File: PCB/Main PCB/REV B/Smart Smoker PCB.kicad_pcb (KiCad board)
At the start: 4 copper layers, 102 parts, among them J1 105017-0001, J10 MEM2051-00-195-00-A, J11 Hopper, J12 Lid, J2 HEATER, J3 393570002, J4 AUGER, J5 393570002, J6 393570002, J7 393570002, J8 393570002, J9 FAN, Q1 25V 1.5A Trans, Q2 25V 1.5A Trans, Q3 Q_PMOS_GSD, Q4 Q_PMOS_GSD, SW1 SW_Coded_SH-7050, U1 AMS1117-3.3, U2 CP2102N-Axx-xQFN20, U3 DG409LEDY-T1-GE3, U4 MAX31855KASA, U5 ESP32-WROOM-32UE_16MB, U6 CPC1966B, U7 AQH2223A, U8 LTC4412xS6, U9 AQH2223A

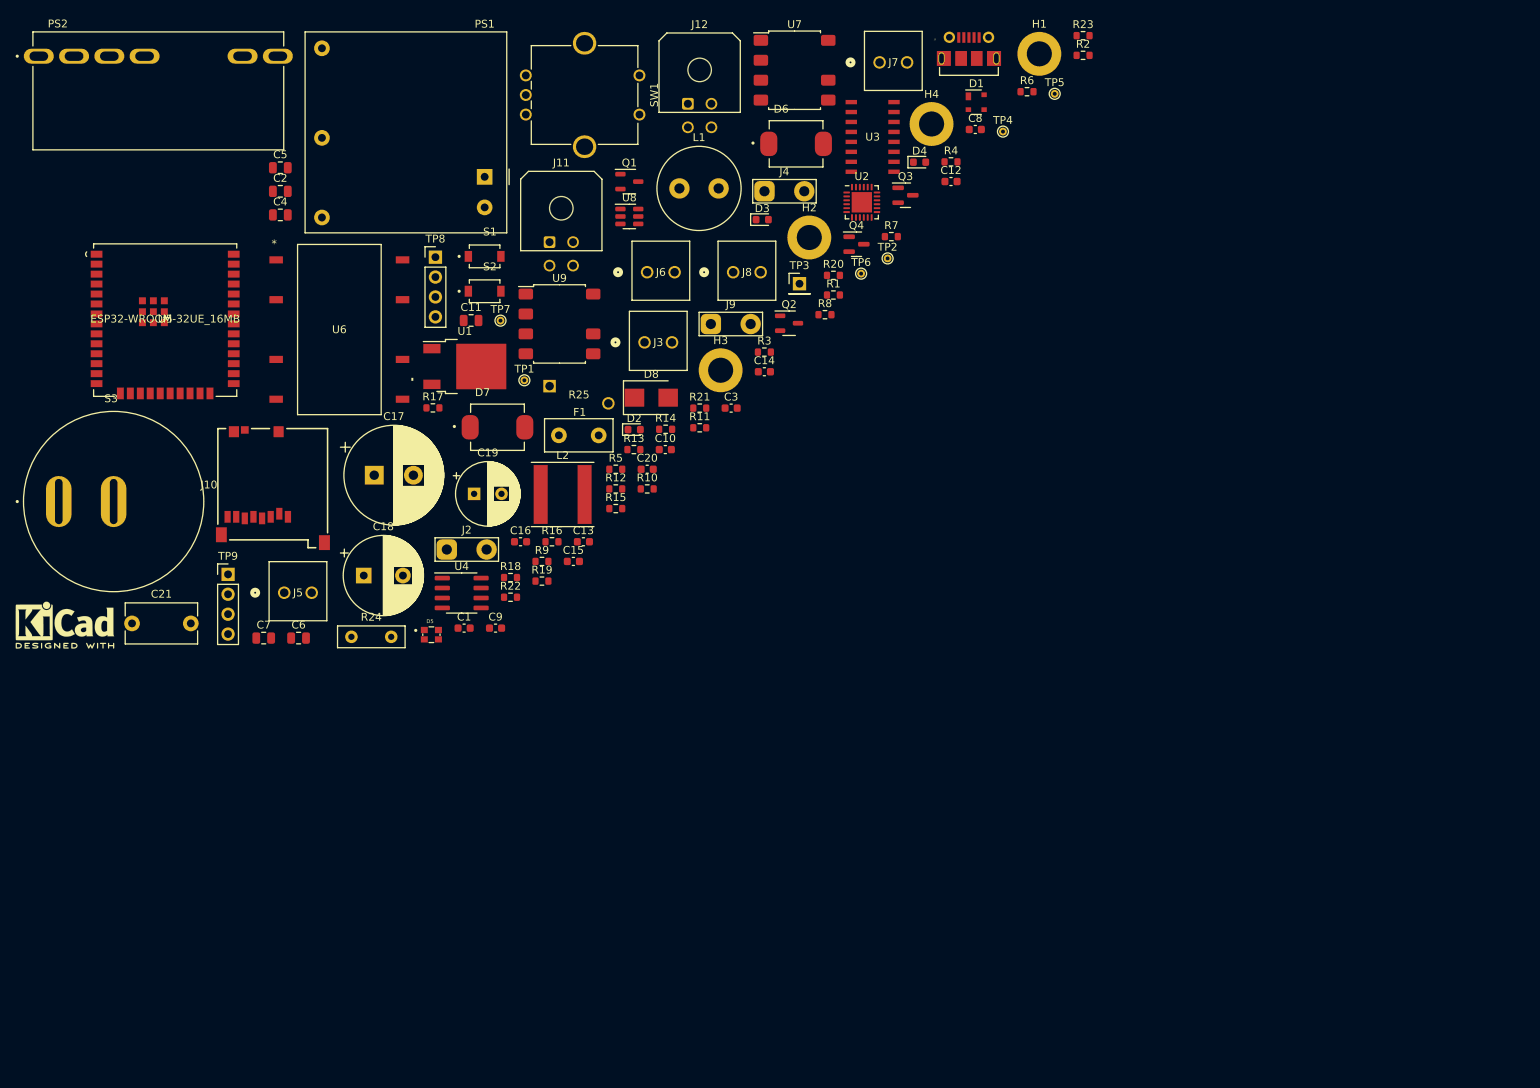
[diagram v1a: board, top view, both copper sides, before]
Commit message: Rev B Hardware - organization of schematic and initial layout for board sizing
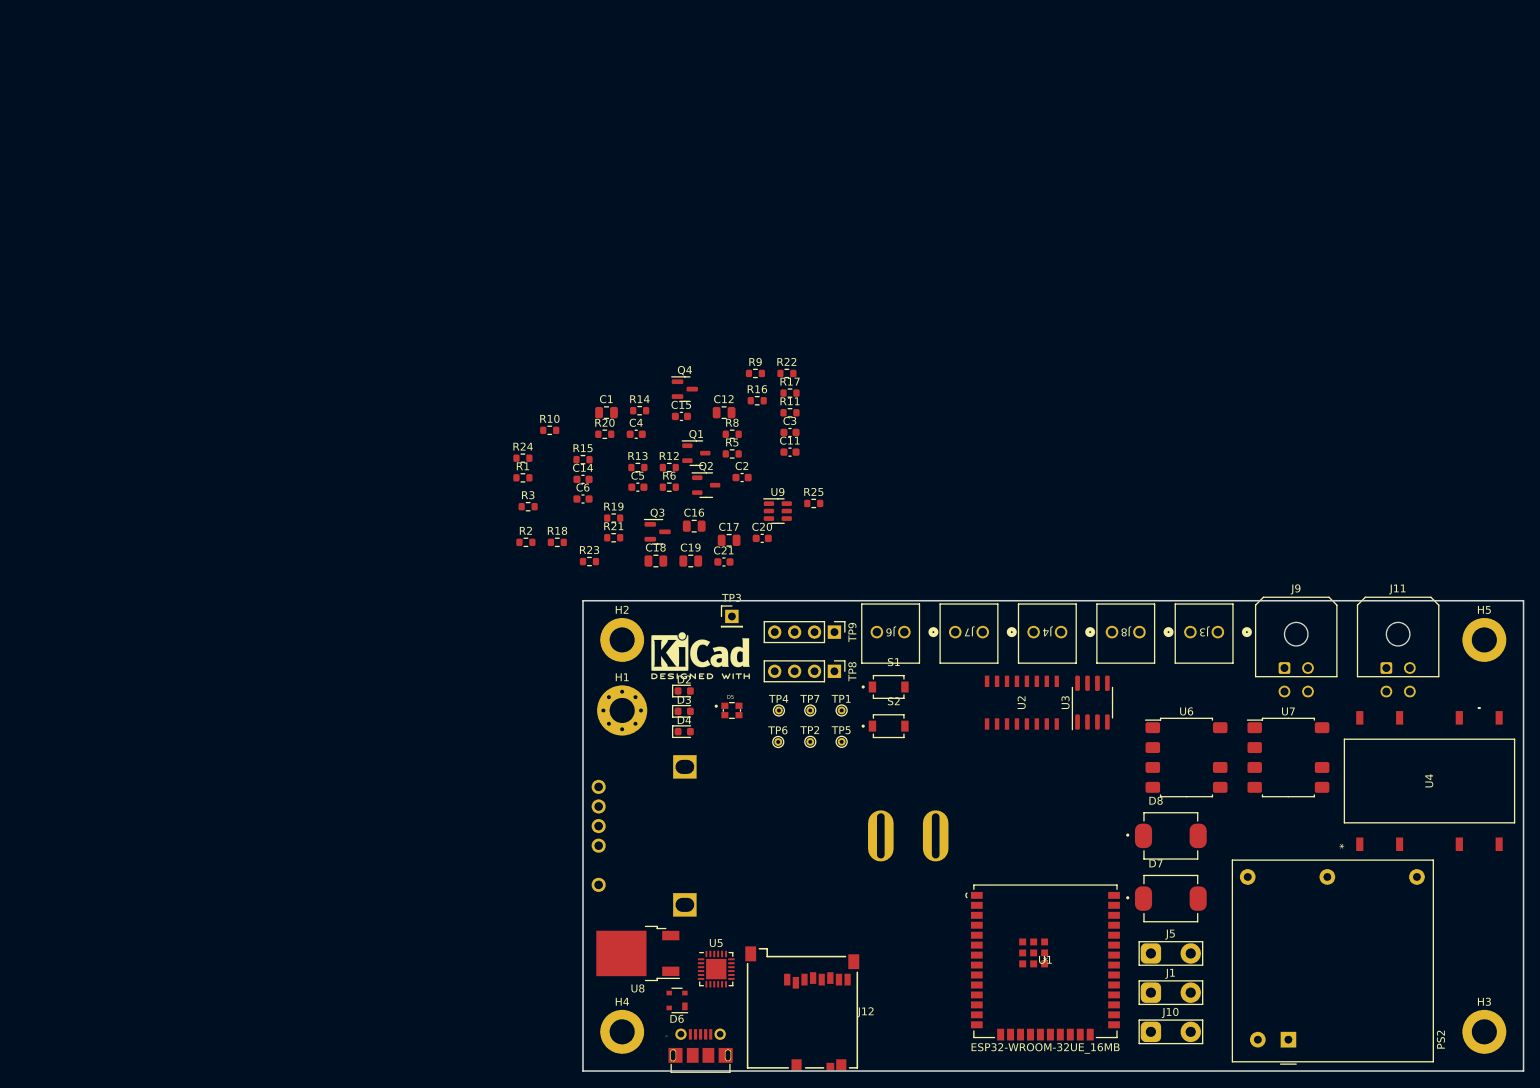
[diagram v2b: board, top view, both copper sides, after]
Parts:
- removed C10: 0.01uF 50V X7R 0603, Capacitor_SMD:C_0603_1608Metric
- removed C13, C8, C9: 0.1uF 50V X7R 0603, Capacitor_SMD:C_0603_1608Metric
- removed C7: 10uF 16V X5R 0805, Capacitor_SMD:C_0805_2012Metric
- removed D1: SP0503BAHT, Package_TO_SOT_SMD:SOT-143
- removed F1: 300V 2A SlowBlow, Fuse:Fuse_Littelfuse_395Series
- removed L1: 2.2mH 500mA 2.5Ohm TH, Inductor_THT:L_Radial_D10.5mm_P5.00mm_Abacron_AISR-01
- removed L2: 2.2uH 7.2A 11.5mOhm, Inductor_SMD:L_Taiyo-Yuden_NR-80xx
- removed PS1: RAC05-3.3SK, Converter_ACDC:Converter_ACDC_RECOM_RAC05-xxSK_THT
- removed R4: 10K 1% 0603, Resistor_SMD:R_0603_1608Metric
- removed R7: 0Ohm 0603, Resistor_SMD:R_0603_1608Metric
- added H5: MountingHole, MountingHole:MountingHole_3.2mm_M3_DIN965_Pad, F.Cu at (215.0, 105.0)
- C1: value 0.1uF 50V X7R 0603 -> 22uF 10V X5R 0805; footprint Capacitor_SMD:C_0603_1608Metric -> Capacitor_SMD:C_0805_2012Metric
- C11: value 22uF 10V X5R 0805 -> 0.1uF 50V X7R 0603; footprint Capacitor_SMD:C_0805_2012Metric -> Capacitor_SMD:C_0603_1608Metric
- C12: value 0.1uF 50V X7R 0603 -> 4.7uF 25V X5R 0805; footprint Capacitor_SMD:C_0603_1608Metric -> Capacitor_SMD:C_0805_2012Metric
- C15: value 1uF 25V X5R 0603 -> 0.1uF 50V X7R 0603
- C16: value 0.1uF 50V X7R 0603 -> 10uF 16V X5R 0805; footprint Capacitor_SMD:C_0603_1608Metric -> Capacitor_SMD:C_0805_2012Metric
- C17: value 22uF 450V 20% -> 10uF 16V X5R 0805; footprint Capacitor_THT:CP_Radial_D12.5mm_P5.00mm -> Capacitor_SMD:C_0805_2012Metric
- C18: value 820uF 20% 16V -> 10uF 16V X5R 0805; footprint Capacitor_THT:CP_Radial_D10.0mm_P5.00mm -> Capacitor_SMD:C_0805_2012Metric
- C19: value 150uF 20% 35V -> 10uF 16V X5R 0805; footprint Capacitor_THT:CP_Radial_D8.0mm_P3.50mm -> Capacitor_SMD:C_0805_2012Metric
- C2: value 4.7uF 25V X5R 0805 -> 0.1uF 50V X7R 0603; footprint Capacitor_SMD:C_0805_2012Metric -> Capacitor_SMD:C_0603_1608Metric
- C20: value 0.1uF 50V X7R 0603 -> 1uF 25V X5R 0603
- C21: value 1000pF 440VAC Y5P -> 0.1uF 50V X7R 0603; footprint Capacitor_THT:C_Disc_D9.0mm_W5.0mm_P7.50mm -> Capacitor_SMD:C_0603_1608Metric
- C4: value 10uF 16V X5R 0805 -> 0.01uF 50V X7R 0603; footprint Capacitor_SMD:C_0805_2012Metric -> Capacitor_SMD:C_0603_1608Metric
- C5, C6: value 10uF 16V X5R 0805 -> 0.1uF 50V X7R 0603; footprint Capacitor_SMD:C_0805_2012Metric -> Capacitor_SMD:C_0603_1608Metric
- D6: value D_TVS -> SP0503BAHT; footprint Customs Smoker:DIOM7959X262N -> Package_TO_SOT_SMD:SOT-143
- D8: value TVS DIODE 7VWM 12VC SMB -> D_TVS; footprint Diode_SMD:D_SMB -> Customs Smoker:DIOM7959X262N
- H1: value MountingHole -> AC_GND; footprint MountingHole:MountingHole_3.2mm_M3_DIN965_Pad -> MountingHole:MountingHole_3.2mm_M3_Pad_Via
- J1: value 105017-0001 -> HEATER; footprint Customs Smoker:MOLEX_105017-0001 -> TestPoint:TestPoint_2Pads_Pitch5.08mm_Drill1.3mm
- J10: value MEM2051-00-195-00-A -> FAN; footprint Customs Smoker:GCT_MEM2051-00-195-00-A -> TestPoint:TestPoint_2Pads_Pitch5.08mm_Drill1.3mm
- J11: value Hopper -> Lid
- J12: value Lid -> MEM2051-00-195-00-A; footprint Connector_Molex:Molex_Micro-Fit_3.0_43045-0400_2x02_P3.00mm_Horizontal -> Customs Smoker:GCT_MEM2051-00-195-00-A
- J2: value HEATER -> 105017-0001; footprint TestPoint:TestPoint_2Pads_Pitch5.08mm_Drill1.3mm -> Customs Smoker:MOLEX_105017-0001
- J4: value AUGER -> 393570002; footprint TestPoint:TestPoint_2Pads_Pitch5.08mm_Drill1.3mm -> Customs Smoker:CONN_393570002_MOL
- J5: value 393570002 -> AUGER; footprint Customs Smoker:CONN_393570002_MOL -> TestPoint:TestPoint_2Pads_Pitch5.08mm_Drill1.3mm
- J9: value FAN -> Hopper; footprint TestPoint:TestPoint_2Pads_Pitch5.08mm_Drill1.3mm -> Connector_Molex:Molex_Micro-Fit_3.0_43045-0400_2x02_P3.00mm_Horizontal
- PS2: value LS10-13B03R3 -> RAC05-3.3SK; footprint Customs Smoker:CONV_LS10-13B03R3 -> Converter_ACDC:Converter_ACDC_RECOM_RAC05-xxSK_THT
- R1: value 1kOhm 1% 0603 -> 1.8kOhm 1% 0603
- R11: value 470Ohm 1% 0603 -> 750Ohm 1% 0603
- R13: value 140Ohm 1% 0603 -> 22.1kOhm 1% 0603
- R14: value 750Ohm 1% 0603 -> 20Ohm 1% 0603
- R15: value 80.6Ohm 1% 0603 -> 20Ohm 1% 0603
- R16: value 20Ohm 1% 0603 -> 80.6Ohm 1% 0603
- R17: value 20Ohm 1% 0603 -> 64.9Ohm 1% 0603
- R18: value 64.9Ohm 1% 0603 -> 0Ohm 0603
- R19: value 140Ohm 1% 0603 -> 47.5kOhm 1% 0603
- R2: value 10K 1% 0603 -> 1.8kOhm 1% 0603
- R20: value 80.6Ohm 1% 0603 -> 0Ohm 0603
- R21: value 470Ohm 5% 0603 -> 140Ohm 1% 0603
- R22: value 140Ohm 1% 0603 -> 80.6Ohm 1% 0603
- R23: value 80.6Ohm 1% 0603 -> 140Ohm 1% 0603
- R24: value 6.8Ohm 3W 5% 2512 -> 80.6Ohm 1% 0603; footprint Resistor_THT:R_Box_L8.4mm_W2.5mm_P5.08mm -> Resistor_SMD:R_0603_1608Metric
- R25: value B72214S0351K101 -> 470Ohm 5% 0603; footprint Customs Smoker:VARS_B72214S_15P5X5P6-7P5-2P2_TDK -> Resistor_SMD:R_0603_1608Metric
- R3: value 22.1kOhm 1% 0603 -> 10K 1% 0603
- R5: value 47.5kOhm 1% 0603 -> 470Ohm 1% 0603
- R6: value 0Ohm 0603 -> 10K 1% 0603
- R8: value 1.8kOhm 1% 0603 -> 1kOhm 1% 0603
- R9: value 1.8kOhm 1% 0603 -> 140Ohm 1% 0603
- S3: moved to B.Cu
- SW1: footprint Rotary_Encoder:RotaryEncoder_Bourns_Vertical_PEC12R-3xxxF-Sxxxx -> Rotary_Encoder:PAC18R1-43D19F; moved to B.Cu
- U1: value AMS1117-3.3 -> ESP32-WROOM-32UE_16MB; footprint Package_TO_SOT_SMD:TO-252-2 -> Customs Smoker:ESP32-WROOM-32UE 16MB
- U2: value CP2102N-Axx-xQFN20 -> DG409LEDY-T1-GE3; footprint Package_DFN_QFN:QFN-24-1EP_4x4mm_P0.5mm_EP2.6x2.6mm -> Customs Smoker:SOIC16_NARROW_VIS
- U3: value DG409LEDY-T1-GE3 -> MAX31855KASA; footprint Customs Smoker:SOIC16_NARROW_VIS -> Package_SO:SOIC-8_3.9x4.9mm_P1.27mm
- U4: value MAX31855KASA -> CPC1966B; footprint Package_SO:SOIC-8_3.9x4.9mm_P1.27mm -> Customs Smoker:CPC1966B_IXY
- U5: value ESP32-WROOM-32UE_16MB -> CP2102N-Axx-xQFN20; footprint Customs Smoker:ESP32-WROOM-32UE 16MB -> Package_DFN_QFN:QFN-24-1EP_4x4mm_P0.5mm_EP2.6x2.6mm
- U6: value CPC1966B -> AQH2223A; footprint Customs Smoker:CPC1966B_IXY -> Package_SO:SSO-7-8_6.4x9.78mm_P2.54mm
- U8: value LTC4412xS6 -> AMS1117-3.3; footprint Package_TO_SOT_SMD:TSOT-23-6 -> Package_TO_SOT_SMD:TO-252-2
- U9: value AQH2223A -> LTC4412xS6; footprint Package_SO:SSO-7-8_6.4x9.78mm_P2.54mm -> Package_TO_SOT_SMD:TSOT-23-6
- moved PS2 191.1 mm to (190.0, 156.0), turned to -90 degrees
- moved J10 131.8 mm to (172.5, 155.0)
- moved H3 128.9 mm to (215.0, 155.0)
- moved U4 125.8 mm to (208.0, 123.0), turned to 90 degrees
- moved H4 122.4 mm to (105.0, 155.0)
- moved J1 121.4 mm to (172.5, 150.0)
- moved U6 121.1 mm to (177.0, 120.0)
- moved J11 119.8 mm to (202.5, 108.6)
- moved J5 119.8 mm to (172.5, 145.0)
- moved J12 116.3 mm to (128.0, 152.0), turned to 180 degrees
- moved D6 110.3 mm to (112.0, 151.0), turned to 180 degrees
- moved U5 108.6 mm to (117.0, 147.0)
- moved U7 108.0 mm to (190.0, 120.0)
- moved S3 106.8 mm to (138.0, 130.0), turned to 180 degrees
- moved U1 106.0 mm to (159.0, 146.0)
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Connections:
- C14 pad 1: /IO0 -> +5V
- C15 pad 2: +3.3V -> +3.3VA
- C17 pad 1: Net-(C17-Pad1) -> +5V
- C17 pad 2: Net-(C17-Pad2) -> GND
- C18 pad 1: Net-(C18-Pad1) -> +3.3VP
- C19 pad 1: +3.3VA -> +3.3VP
- C20 pad 1: +3.3VA -> GND
- C20 pad 2: GND -> +3.3V
- C21 pad 1: Net-(C17-Pad2) -> +3.3VA
- C3 pad 1: Net-(C3-Pad1) -> +3.3V
- C3 pad 2: Net-(C3-Pad2) -> GND
- C4 pad 1: Net-(C3-Pad2) -> /MUX_OUT_+
- C4 pad 2: Net-(C3-Pad1) -> /MUX_OUT_-
- C5 pad 1: +5V -> /EN
- C6 pad 1: +3.3VP -> /IO0
- D6 pad 1: /Auger_+ -> GND
- D6 pad 2: /AC_L -> /USB_DP
- D7 pad 1: /Fan_+ -> /Auger_+
- D8 pad 1: GND -> /Fan_+
- D8 pad 2: +3.3VA -> /AC_L
- H1 pad 1: (no net) -> GND
- J1 pad 1: +5V -> /Heater_+
- J1 pad 2: /USB_DN -> /AC_N
- J10 pad 1: unconnected-(J10-Pad1) -> /Fan_+
- J10 pad 2: unconnected-(J10-Pad2) -> /AC_N
- J12 pad 1: /I2C_SDA -> unconnected-(J12-Pad1)
- J12 pad 2: GND -> unconnected-(J12-Pad2)
- J12 pad 3: /I2C_SCL -> unconnected-(J12-Pad3)
- J12 pad 4: +3.3V -> unconnected-(J12-Pad4)
- J2 pad 1: /Heater_+ -> +5V
- J2 pad 2: /AC_N -> /USB_DN
- J4 pad 1: /Auger_+ -> /AC_L
- J5 pad 1: /AC_L -> /Auger_+
- J9 pad 1: /Fan_+ -> /I2C_SDA
- J9 pad 2: /AC_N -> GND
- PS2 pad 1: /AC_N -> /Power/AC_L
- PS2 pad 2: Net-(L1-Pad2) -> /Power/AC_N
- PS2 pad 3: Net-(C17-Pad1) -> unconnected-(PS2-Pad3)
- PS2 pad 4: Net-(C17-Pad2) -> GND
- PS2 pad 5: GND -> +3.3VA
- Q3 pad 1: /IO4 -> /Power/IO4
- Q4 pad 1: Net-(U8-Pad5) -> Net-(Q4-Pad1)
- R1 pad 1: Net-(R1-Pad1) -> /I2C_SCL
- R10 pad 1: /EN -> /RTS
- R10 pad 2: +3.3V -> Net-(Q2-Pad2)
- R11 pad 2: Net-(D2-Pad2) -> Net-(D4-Pad2)
- R12 pad 1: +5V -> unconnected-(R12-Pad1)
- R12 pad 2: Net-(D3-Pad2) -> Net-(R12-Pad2)
- R13 pad 1: unconnected-(R13-Pad1) -> +5V
- R14 pad 1: +3.3V -> Net-(D5-Pad3)
- R14 pad 2: Net-(D4-Pad2) -> /IO26
- R15 pad 1: Net-(R13-Pad2) -> Net-(D5-Pad4)
- R15 pad 2: GND -> /IO27
- R16 pad 1: Net-(D5-Pad3) -> Net-(R12-Pad2)
- R16 pad 2: /IO26 -> GND
- R17 pad 1: Net-(D5-Pad4) -> Net-(D5-Pad2)
- R17 pad 2: /IO27 -> /IO25
- R18 pad 1: Net-(D5-Pad2) -> /TXD0
- R18 pad 2: /IO25 -> /RXD
- R19 pad 1: unconnected-(R19-Pad1) -> GND
- R19 pad 2: Net-(R19-Pad2) -> Net-(R13-Pad2)
- R2 pad 1: /DTR -> /I2C_SDA
- R2 pad 2: Net-(Q1-Pad2) -> +3.3V
- R20 pad 1: Net-(R19-Pad2) -> /RXD0
- R20 pad 2: GND -> /TXD
- R21 pad 1: /IO4 -> unconnected-(R21-Pad1)
- R21 pad 2: +3.3V -> Net-(R21-Pad2)
- R22 pad 1: unconnected-(R22-Pad1) -> Net-(R21-Pad2)
- R22 pad 2: Net-(R22-Pad2) -> GND
- R23 pad 1: Net-(R22-Pad2) -> unconnected-(R23-Pad1)
- R23 pad 2: GND -> Net-(R23-Pad2)
- R24 pad 1: Net-(F1-Pad2) -> Net-(R23-Pad2)
- R24 pad 2: Net-(L1-Pad1) -> GND
- R25 pad 1: Net-(F1-Pad2) -> /Power/IO4
- R25 pad 2: /AC_N -> +3.3V
- R3 pad 1: +5V -> /EN
- R3 pad 2: Net-(R3-Pad2) -> +3.3V
- R5 pad 1: GND -> +3.3V
- R5 pad 2: Net-(R3-Pad2) -> Net-(D2-Pad2)
- R6 pad 1: /TXD0 -> /DTR
- R6 pad 2: /RXD -> Net-(Q1-Pad2)
- R8 pad 1: /I2C_SCL -> Net-(R8-Pad1)
- R9 pad 1: /I2C_SDA -> +5V
- R9 pad 2: +3.3V -> Net-(D3-Pad2)
- U1 pad 2: +3.3VP -> +3.3V
- U1 pad 3: +5V -> /EN
- U2 pad 1: unconnected-(U2-Pad1) -> /IO2
- U2 pad 10: unconnected-(U2-Pad10) -> /Probe4+
- U2 pad 11: unconnected-(U2-Pad11) -> /Probe3+
- U2 pad 12: unconnected-(U2-Pad12) -> /Probe2+
- U2 pad 13: unconnected-(U2-Pad13) -> /Probe1+
- U2 pad 14: unconnected-(U2-Pad14) -> +3.3V
- U2 pad 15: unconnected-(U2-Pad15) -> GND
- U2 pad 16: unconnected-(U2-Pad16) -> /IO15
- U2 pad 2: GND -> +3.3V
- U2 pad 3: /USB_DP -> GND
- U2 pad 4: /USB_DN -> /Probe1-
- U2 pad 5: +3.3V -> /Probe2-
- U2 pad 6: +3.3V -> /Probe3-
- U2 pad 7: +3.3V -> /Probe4-
- U2 pad 8: Net-(R3-Pad2) -> /MUX_OUT_-
- U2 pad 9: Net-(R1-Pad1) -> /MUX_OUT_+
- U3 pad 1: /IO2 -> GND
- U3 pad 2: +3.3V -> /MUX_OUT_-
- U3 pad 3: GND -> /MUX_OUT_+
- U3 pad 4: /Probe1- -> +3.3V
- U3 pad 5: /Probe2- -> /SPI_SCK
- U3 pad 6: /Probe3- -> /SPI_CS
- U3 pad 7: /Probe4- -> /SPI_MISO
- U3 pad 8: /MUX_OUT_- -> (no net)
- U4 pad 1: GND -> unconnected-(U4-Pad1)
- U4 pad 2: /MUX_OUT_- -> Net-(R12-Pad2)
- U4 pad 3: /MUX_OUT_+ -> GND
- U4 pad 4: +3.3V -> unconnected-(U4-Pad4)
- U4 pad 5: /SPI_SCK -> /AC_L
- U4 pad 6: /SPI_CS -> /AC_L
- U4 pad 7: /SPI_MISO -> /Heater_+
- U4 pad 8: (no net) -> /Heater_+
- U5 pad 1: GND -> unconnected-(U5-Pad1)
- U5 pad 10: /IO25 -> unconnected-(U5-Pad10)
- U5 pad 11: /IO26 -> unconnected-(U5-Pad11)
- U5 pad 12: /IO27 -> unconnected-(U5-Pad12)
- U5 pad 13: /IO14 -> unconnected-(U5-Pad13)
- U5 pad 14: /IO12 -> unconnected-(U5-Pad14)
- U5 pad 15: GND -> unconnected-(U5-Pad15)
- U5 pad 16: /IO13 -> unconnected-(U5-Pad16)
- U5 pad 18: unconnected-(U5-Pad18) -> /CTS
- U5 pad 19: unconnected-(U5-Pad19) -> /RTS
- U5 pad 2: +3.3V -> GND
- U5 pad 20: unconnected-(U5-Pad20) -> /RXD
- U5 pad 21: unconnected-(U5-Pad21) -> /TXD
- U5 pad 23: /IO15 -> /DTR
- U5 pad 24: /IO2 -> unconnected-(U5-Pad24)
- U5 pad 25: /IO0 -> GND
- U5 pad 3: /EN -> /USB_DP
- U5 pad 4: /I36 -> /USB_DN
- U5 pad 5: /I39 -> +3.3V
- U5 pad 6: /I34 -> +3.3V
- U5 pad 7: /I35 -> +3.3V
- U5 pad 8: /IO32 -> Net-(R13-Pad2)
- U5 pad 9: /IO33 -> Net-(R8-Pad1)
- U6 pad 1: unconnected-(U6-Pad1) -> GND
- U6 pad 2: Net-(R13-Pad2) -> Net-(R21-Pad2)
- U6 pad 4: unconnected-(U6-Pad4) -> GND
- U6 pad 5: /AC_L -> unconnected-(U6-Pad5)
- U6 pad 8: /Heater_+ -> /Auger_+
- U7 pad 2: Net-(R19-Pad2) -> Net-(R23-Pad2)
- U7 pad 8: /Auger_+ -> /Fan_+
- U8 pad 1: +3.3VA -> GND
- U8 pad 2: GND -> +3.3VP
- U8 pad 3: GND -> +5V
- U9 pad 1: GND -> +3.3VA
- U9 pad 2: Net-(R22-Pad2) -> GND
- U9 pad 4: GND -> /Power/IO4
- U9 pad 5: unconnected-(U9-Pad5) -> Net-(Q4-Pad1)
- U9 pad 6: /AC_L -> +3.3V
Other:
- board outline added: 120 x 60 mm

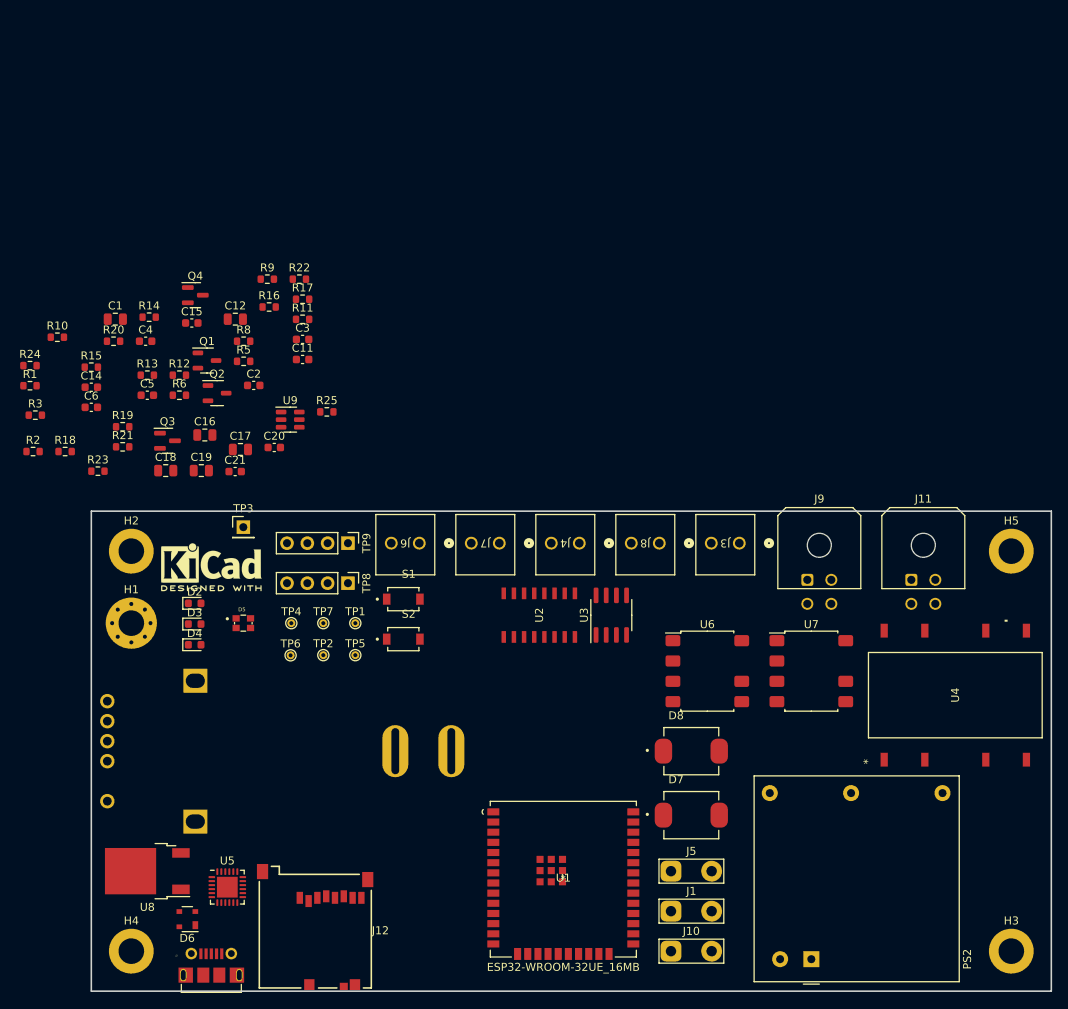
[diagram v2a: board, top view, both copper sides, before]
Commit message: Rid power path selector, moving to or diode system for power path selection
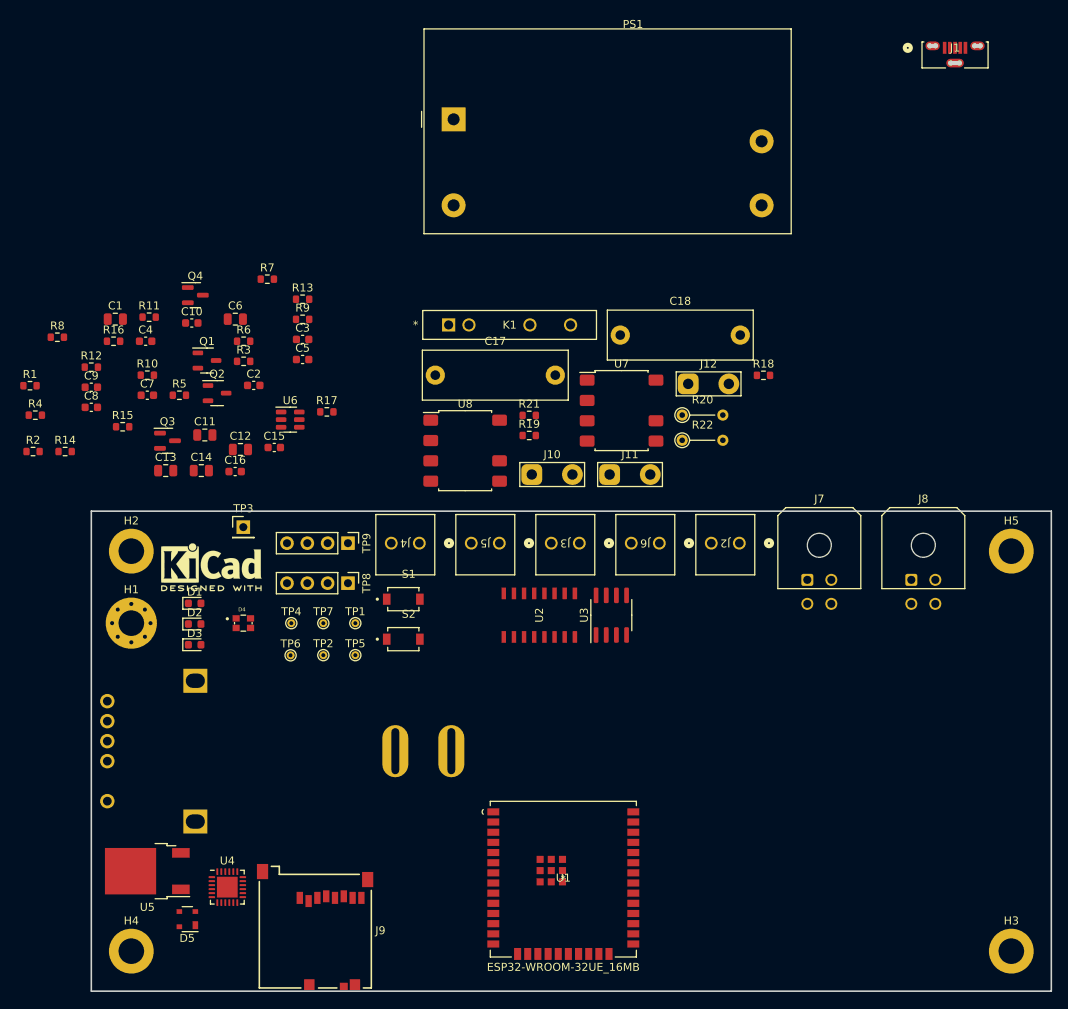
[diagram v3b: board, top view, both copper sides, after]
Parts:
- removed D7, D8: D_TVS, Customs Smoker:DIOM7959X262N
- removed the J2 at (115.0, 158.0)
- removed the J5 at (172.5, 145.0)
- removed PS2: RAC05-3.3SK, Converter_ACDC:Converter_ACDC_RECOM_RAC05-xxSK_THT
- removed the R12 at (111.0, 83.0)
- removed the R16 at (122.2, 74.5)
- removed R23: 140Ohm 1% 0603, Resistor_SMD:R_0603_1608Metric
- removed R24: 80.6Ohm 1% 0603, Resistor_SMD:R_0603_1608Metric
- removed the U4 at (208.0, 123.0)
- removed the U6 at (177.0, 120.0)
- added C17: Film 0.1uF 305V 15mm, Capacitor_THT:C_Rect_L18.0mm_W6.0mm_P15.00mm_FKS3_FKP3, F.Cu at (143.0, 83.0)
- added C18: Film 0.1uF 305V 15mm, Capacitor_THT:C_Rect_L18.0mm_W6.0mm_P15.00mm_FKS3_FKP3, F.Cu at (166.1, 78.0)
- added J11: Auger, TestPoint:TestPoint_2Pads_Pitch5.08mm_Drill1.3mm, F.Cu at (164.8, 95.4)
- added J12: FAN, TestPoint:TestPoint_2Pads_Pitch5.08mm_Drill1.3mm, F.Cu at (174.6, 84.1)
- added K1: CPC1966Y, Customs Smoker:SIP4_CPC1966Y_LTF, F.Cu at (144.7, 76.7)
- added PS1: IRM-10-3.3, Converter_ACDC:Converter_ACDC_MeanWell_IRM-10-xx_THT, F.Cu at (145.3, 51.0)
- added R18: 105Ohm 1% 0603, Resistor_SMD:R_0603_1608Metric, F.Cu at (184.0, 83.0)
- added R19: 105Ohm 1% 0603, Resistor_SMD:R_0603_1608Metric, F.Cu at (154.7, 90.5)
- added R20: 47Ohm 5% 1/2W, Resistor_THT:R_Axial_DIN0204_L3.6mm_D1.6mm_P5.08mm_Vertical, F.Cu at (173.9, 88.0)
- added U8: AQH3223A, Package_SO:SSO-7-8_6.4x9.78mm_P2.54mm, F.Cu at (146.7, 92.4)
- J1: value HEATER -> 1051330001; footprint TestPoint:TestPoint_2Pads_Pitch5.08mm_Drill1.3mm -> Customs Smoker:1051330001_MOL
- J10: value FAN -> Ignitor
- R21: value 140Ohm 1% 0603 -> 105Ohm 1% 0603
- R22: value 80.6Ohm 1% 0603 -> 47Ohm 5% 1/2W; footprint Resistor_SMD:R_0603_1608Metric -> Resistor_THT:R_Axial_DIN0204_L3.6mm_D1.6mm_P5.08mm_Vertical
- U7: value AQH2223A -> AQH3223A
- moved J1 112.8 mm to (208.0, 43.0)
- moved J10 62.1 mm to (155.1, 95.4)
- moved R22 51.9 mm to (173.9, 91.1)
- moved R21 51.0 mm to (154.7, 88.0)
- moved U7 40.3 mm to (166.3, 87.4)
- renumbered C15 to C10, C16 to C11, C17 to C12, C18 to C13, C19 to C14, C20 to C15, C21 to C16, C11 to C5, C12 to C6, C5 to C7, C6 to C8, C14 to C9, D2 to D1, D3 to D2, D4 to D3, D5 to D4, D6 to D5, J3 to J2, J4 to J3, J6 to J4, J7 to J5, J8 to J6, J9 to J7, J11 to J8, J12 to J9, R13 to R10, R14 to R11, R15 to R12, R17 to R13, R18 to R14, R19 to R15, R20 to R16, R25 to R17, R5 to R3, R3 to R4, R6 to R5, R8 to R6, R9 to R7, R10 to R8, R11 to R9, U5 to U4, U8 to U5, U9 to U6
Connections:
- J1 pad 1: /Heater_+ -> +5V
- J1 pad 2: /AC_N -> /USB_DN
- J10 pad 1: /Fan_+ -> /Loads/Heater_+
- J10 pad 2: /AC_N -> /Loads/Auger_-
- R21 pad 1: unconnected-(R21-Pad1) -> /Loads/FAN
- R22 pad 1: Net-(R21-Pad2) -> Net-(C18-Pad2)
- R22 pad 2: GND -> /Loads/AC_N
- U7 pad 6: /AC_L -> /Loads/AC_N
- U7 pad 8: /Fan_+ -> /Loads/Auger_+
